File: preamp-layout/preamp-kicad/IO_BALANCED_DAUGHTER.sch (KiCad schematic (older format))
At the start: 55 parts, among them J82 XLR3, J83 XLR3, J84 Conn_01x03_Male, J85 Conn_01x03_Male, J86 Conn_01x03_Female, J87 Conn_01x03_Male, J88 XLR3, J89 XLR3, U21 TL072, U22 TL072, U23 TL072

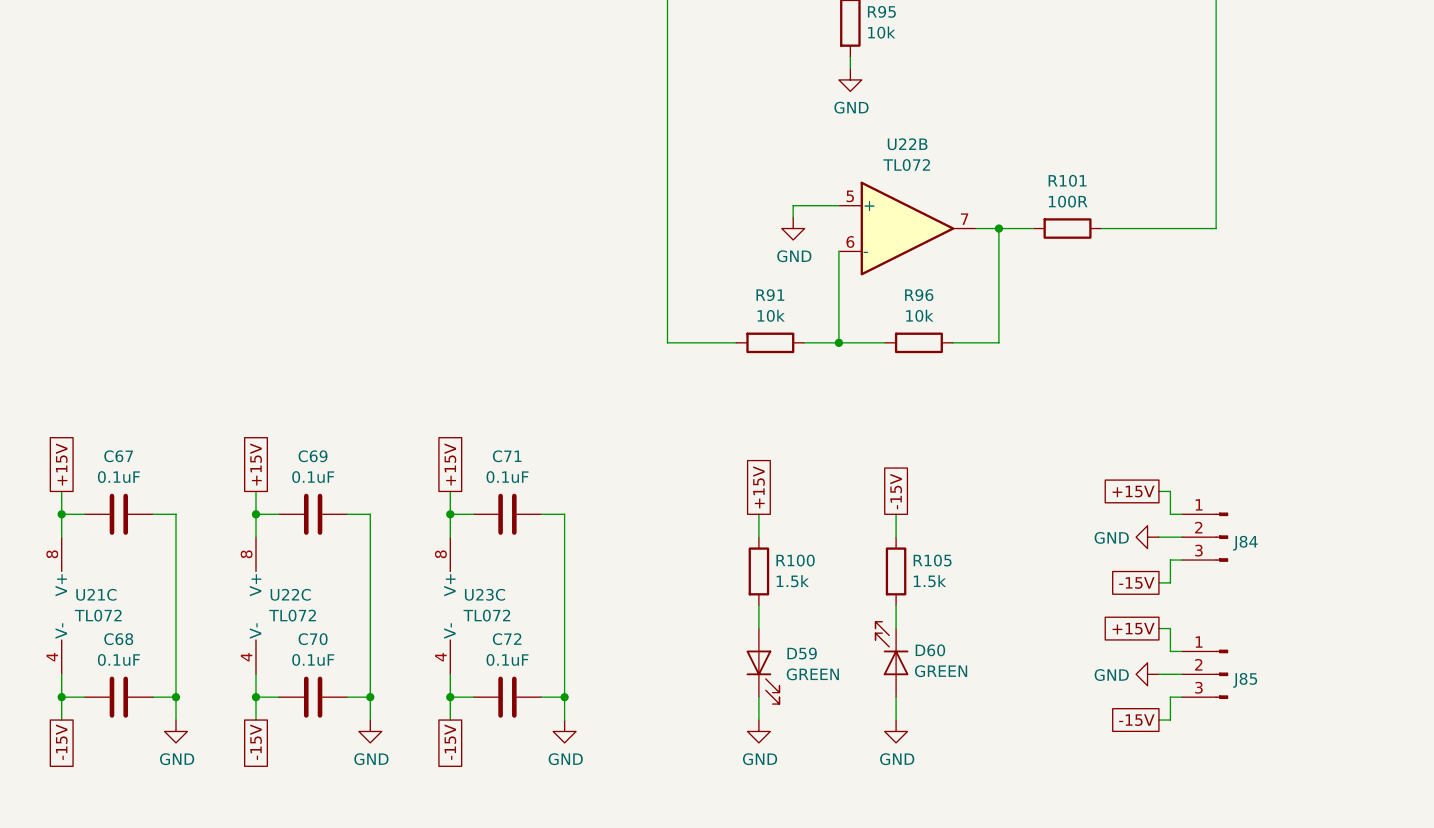
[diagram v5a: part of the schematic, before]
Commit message: Headphone Amp Update
Removed IC buffer on headphone amp schematic. Reconfigured connectors to crossfeed board so that input/output can be easily jumpered.
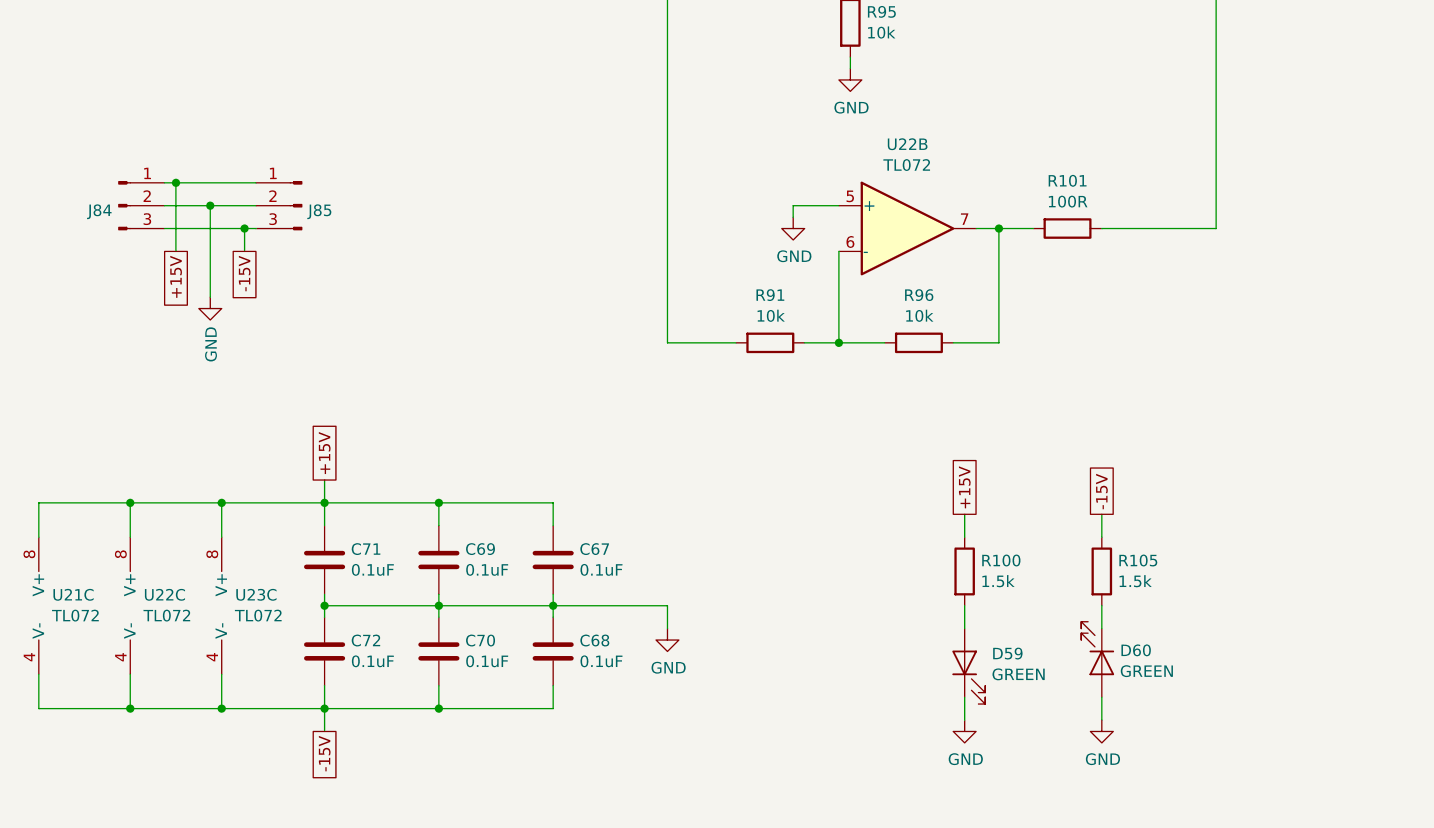
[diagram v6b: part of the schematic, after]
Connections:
- net -15V: now also C68.2, C70.2, C72.2; no longer C68.1, C70.1, C72.1
- net GND: now also C68.1, C70.1, C72.1; no longer C68.2, C70.2, C72.2
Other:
- moved on the sheet: C67, C68, C69, C70, C71, C72, D59, D60, J84, J85, R100, R105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

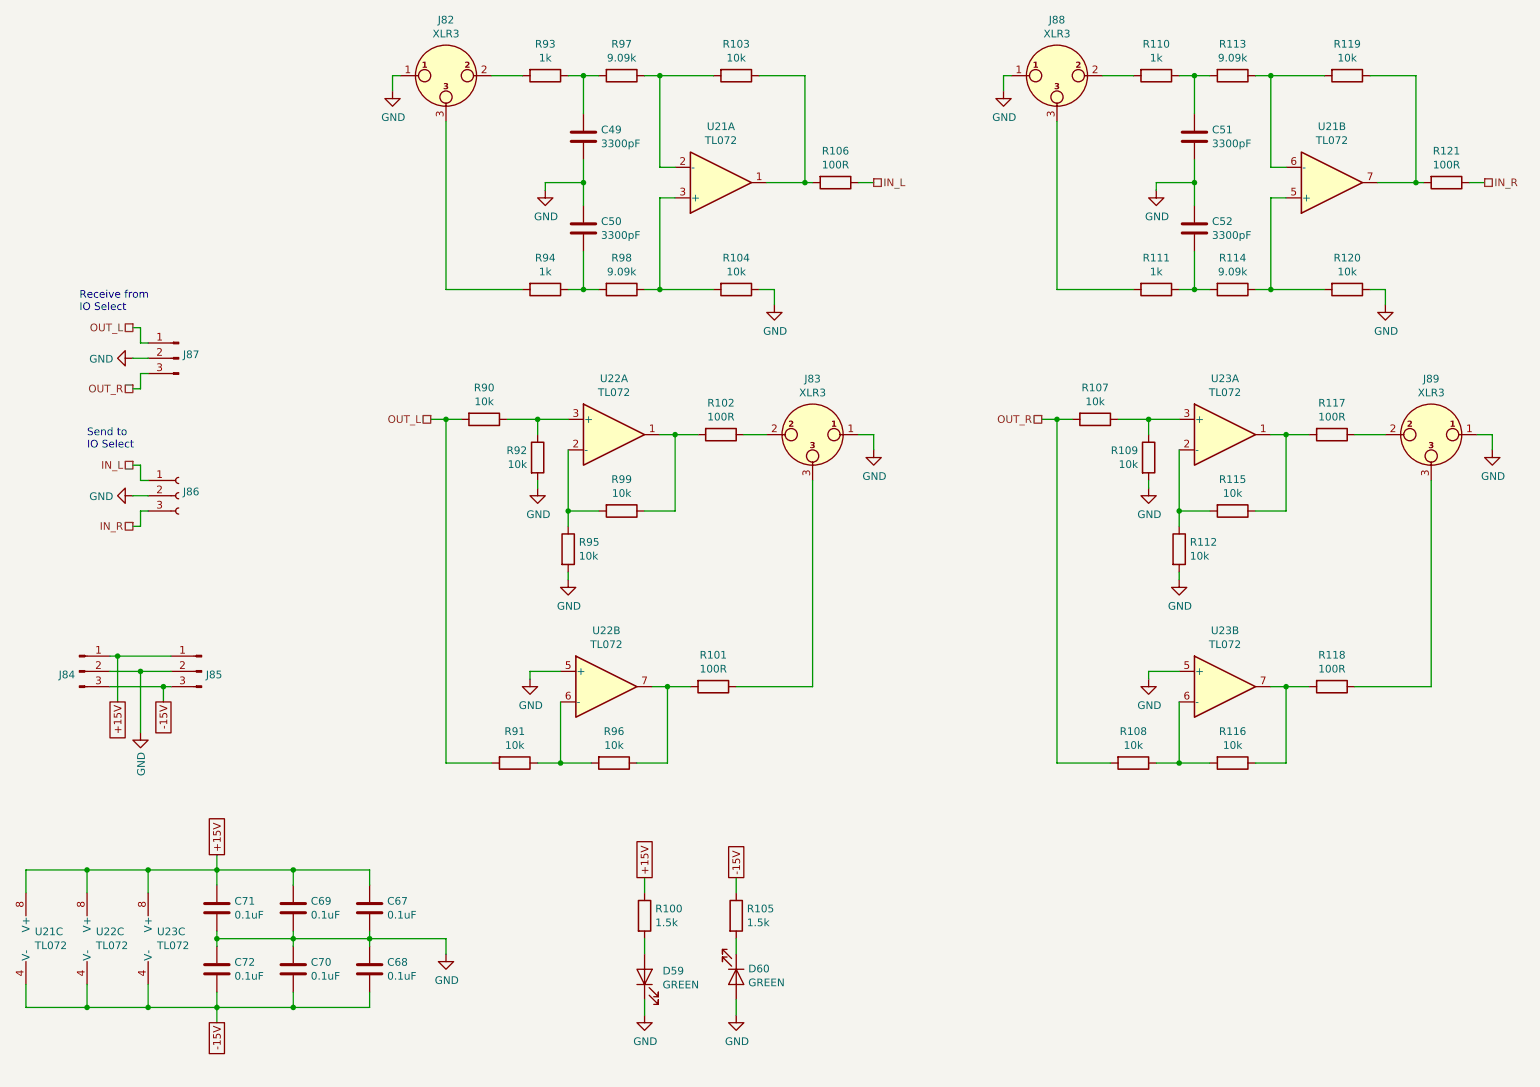
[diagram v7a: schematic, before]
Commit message: Op Amp change up
Changed DAC output buffer to quad TL074 instead of separate TL072 ICs. Changed signal path ICs from generic TL072 to NJM2068M. Updated footprints, BOM, schematic.
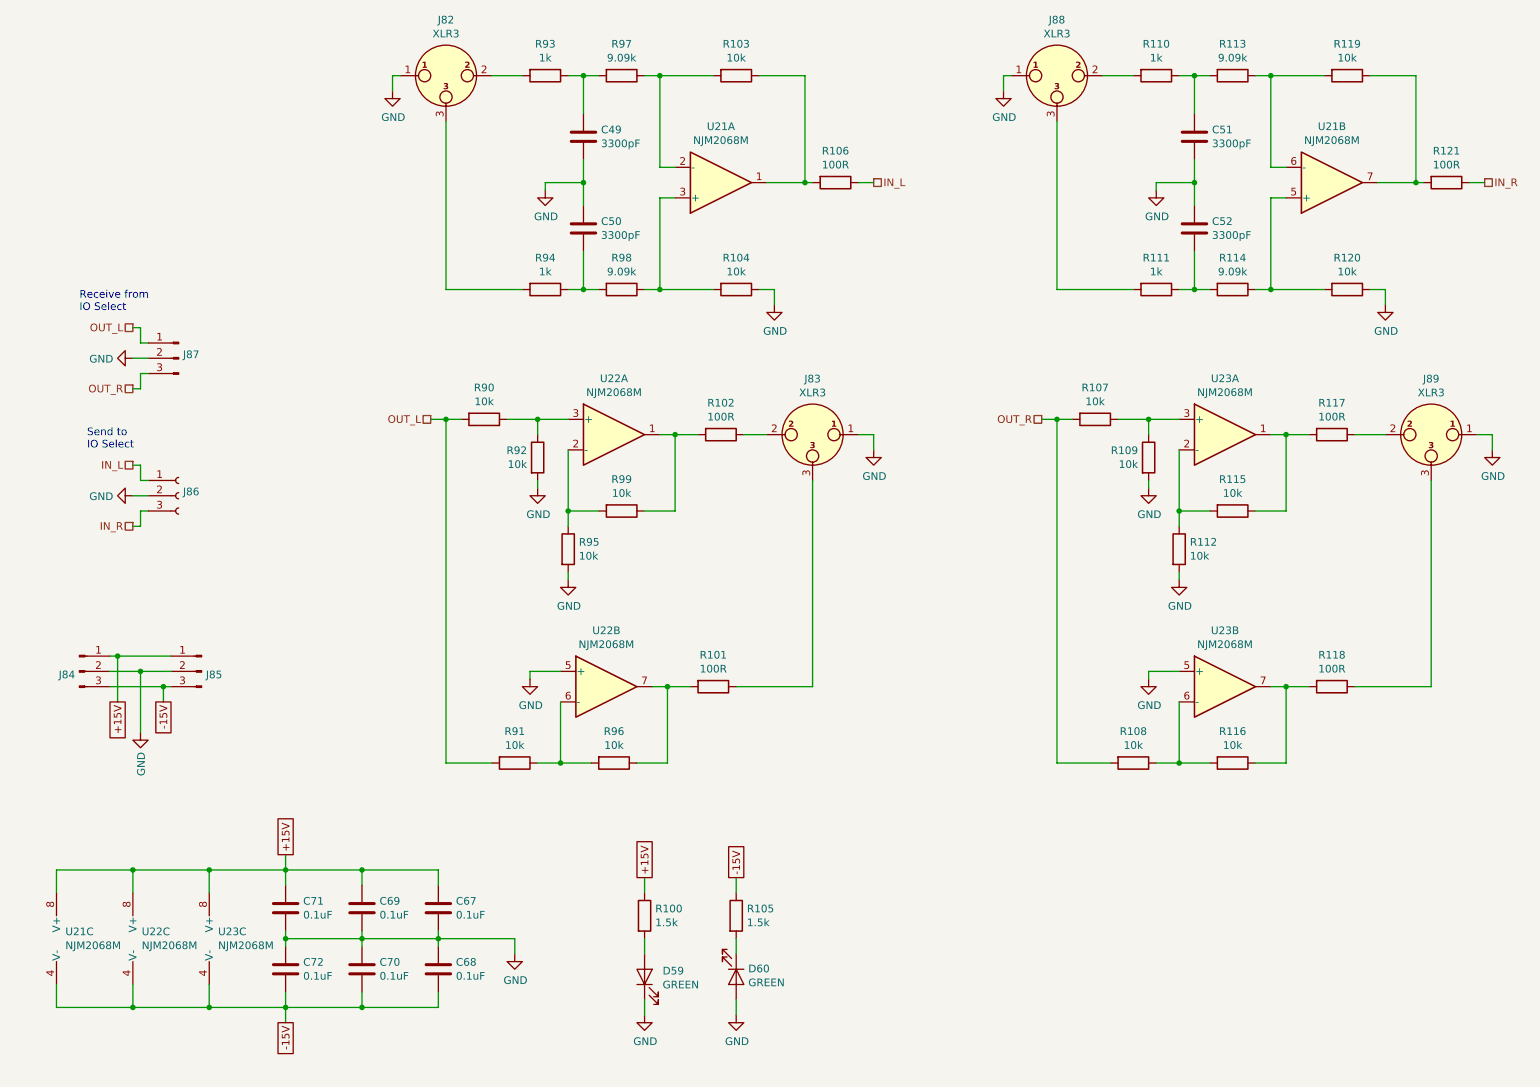
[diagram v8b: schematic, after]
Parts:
- U21, U22, U23: value TL072 -> NJM2068M; footprint Package_DIP:DIP-8_W7.62mm_Socket_LongPads -> Package_SO:SOP-8_3.9x4.9mm_P1.27mm
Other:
- moved on the sheet: C67, C68, C69, C70, C71, C72, U21C, U22C, U23C
